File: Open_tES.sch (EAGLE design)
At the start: 61 parts, among them IC2 MAX232ECWES, IC3 4023D, IC4 LP2950CZ-5.0, IC5 OPA277U, IC6 LF444CM, IC7 PIC16F1937P, U1 MIC2288YD5-TR, U2 ICL7660ACPAZ, X1 22-23-2041, X2 057-016-1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

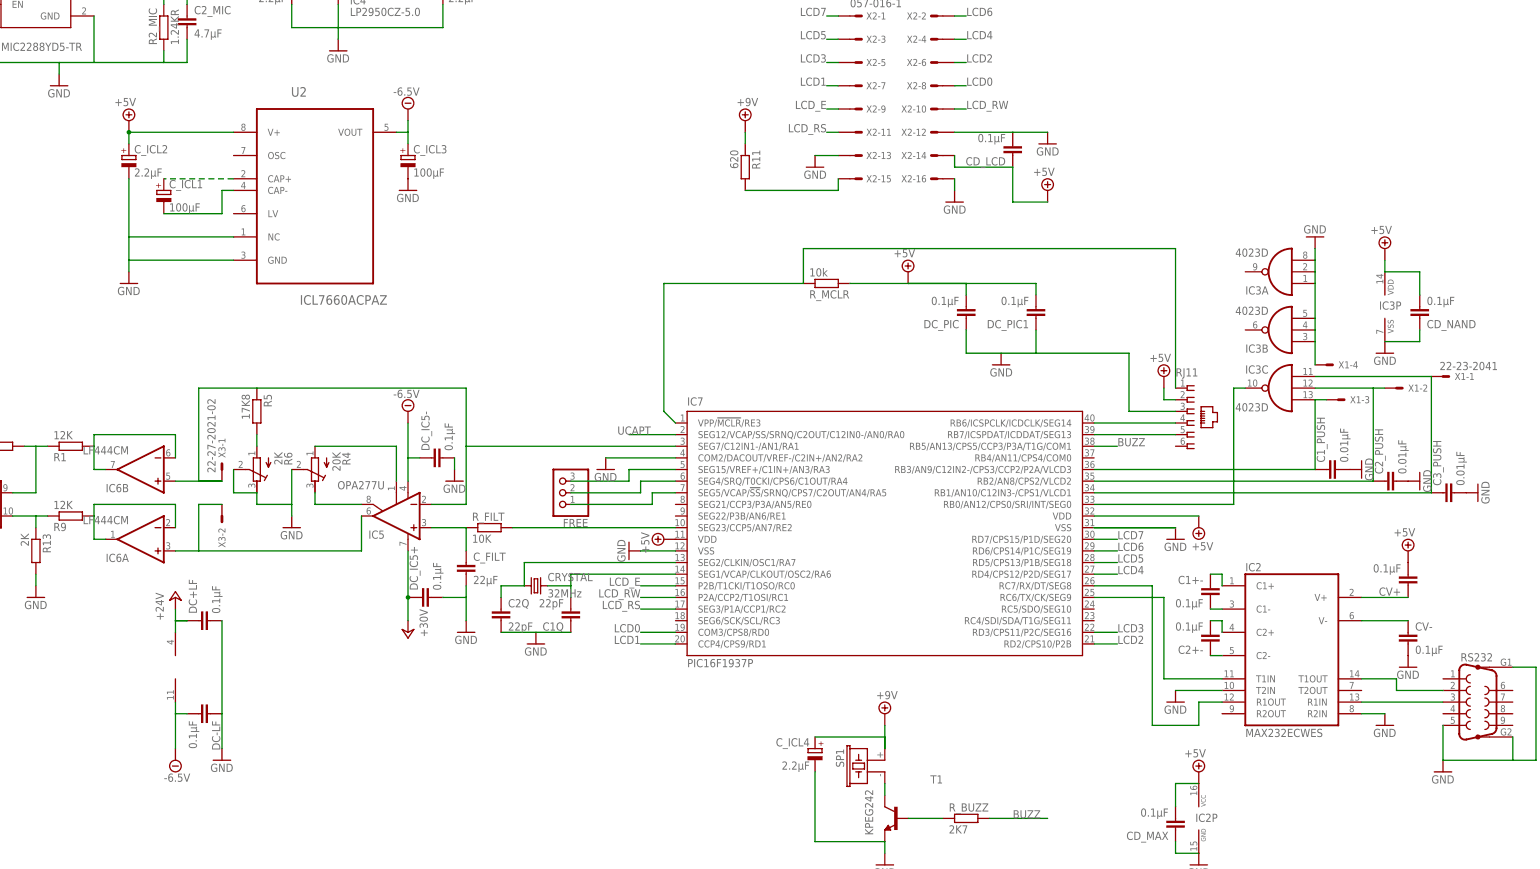
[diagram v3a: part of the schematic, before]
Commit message: use of MAX232 for negative voltage with MIC5270 for regulation (-5V)
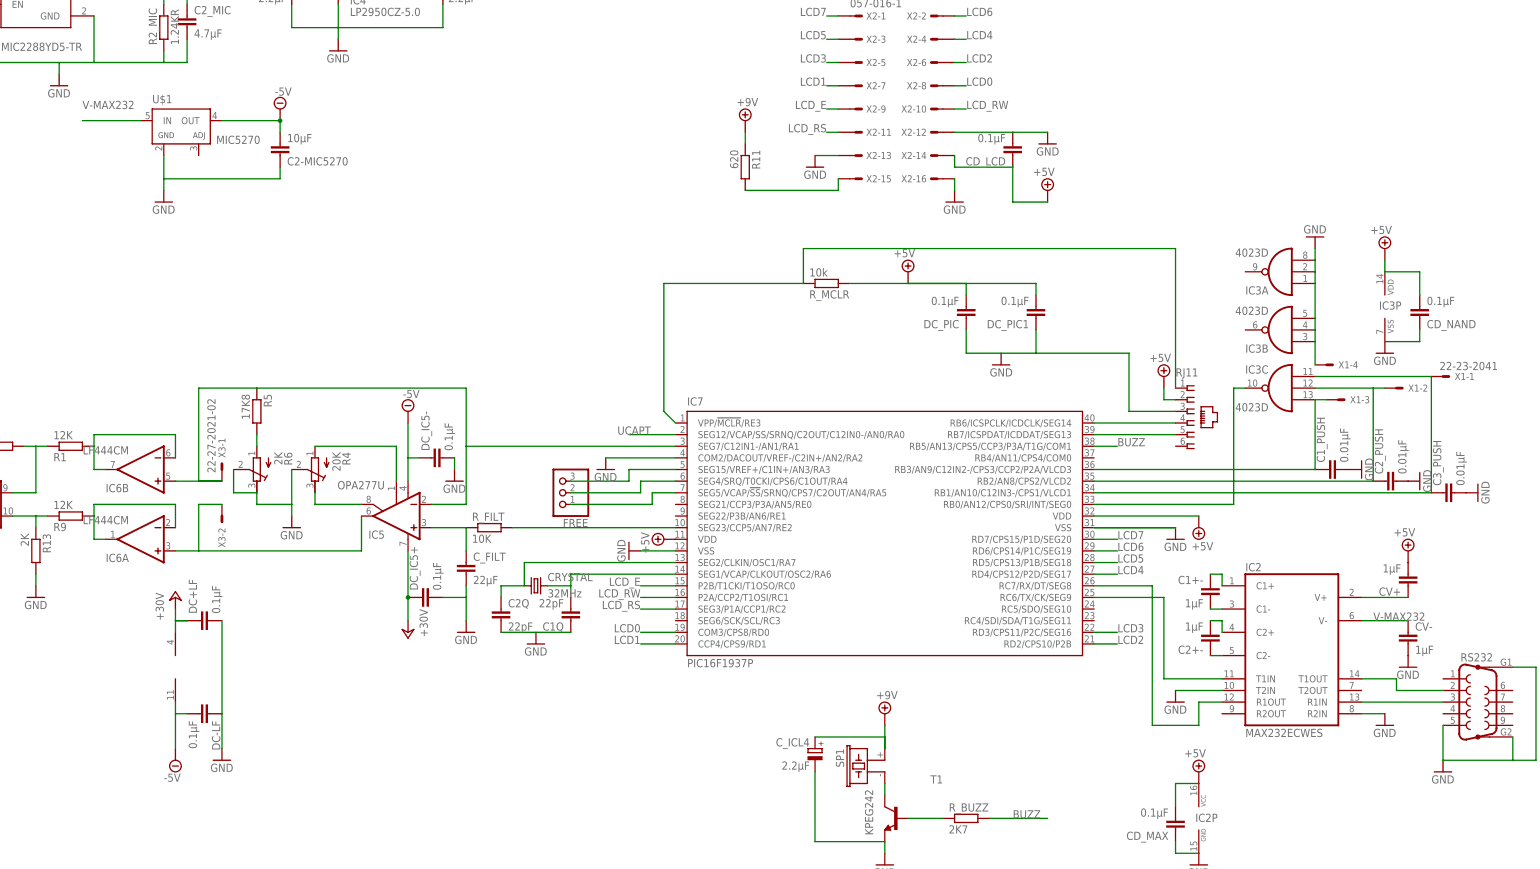
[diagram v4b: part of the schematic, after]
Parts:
- removed C_ICL1, C_ICL3: 100µF, rcl:CPOL-EUE2,5-6E
- removed C_ICL2: 2.2µF, rcl:CPOL-EUE1.8-4
- removed U2: ICL7660ACPAZ, Intersil-ICL7660:ICL7660ACPAZ
- added C2-MIC5270: 10µF, rcl:C-EUC0805
- added U$1: MIC5270, Open_tES:MIC5270
- C1+-, C2+-, CV+, CV-: value 0.1µF -> 1µF; OC_FARNELL 1414664 -> 2496946
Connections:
- removed net N$21: C_ICL1.+, U2.CAP+
- removed net N$27: C_ICL1.-, U2.CAP-
- removed net N$33: CV-.1, IC2G$1.V-
- new net V-MAX232: CV-.1, IC2G$1.V-, U$1.IN
- net +5V/1: no longer C_ICL2.+, U2.V+
- net -5V: now also C2-MIC5270.2, U$1.OUT; no longer C_ICL3.+, U2.VOUT
- net GND: now also C2-MIC5270.1, U$1.GND; no longer C_ICL2.-, C_ICL3.-, U2.GND, U2.NC
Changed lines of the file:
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@@
 <part name="GND13" library="supply1" deviceset="GND" device=""/>
 <part name="GND19" library="supply1" deviceset="GND" device=""/>
-<part name="P+11" library="supply1" deviceset="+24V" device=""/>
+<part name="P+11" library="supply1" deviceset="+24V" device="" value="+30V"/>
 <part name="GND22" library="supply1" deviceset="GND" device=""/>
 <part name="GND25" library="supply1" deviceset="GND" device=""/>
@@
 <attribute name="OC_FARNELL" value="9489479"/>
 </part>
-<part name="U2" library="Intersil-ICL7660" deviceset="ICL7660ACPAZ" device=""/>
-<part name="C_ICL2" library="rcl" deviceset="CPOL-EU" device="E1.8-4" value="2.2µF">
-<attribute name="OC_FARNELL" value="8766983"/>
-</part>
-<part name="GND32" library="supply1" deviceset="GND" device=""/>
-<part name="C_ICL1" library="rcl" deviceset="CPOL-EU" device="E2,5-6E" value="100µF">
-<attribute name="OC_FARNELL" value="9452648"/>
-</part>
-<part name="C_ICL3" library="rcl" deviceset="CPOL-EU" device="E2,5-6E" value="100µF">
-<attribute name="OC_FARNELL" value="9452648"/>
-</part>
-<part name="GND33" library="supply1" deviceset="GND" device=""/>
-<part name="SUPPLY8" library="supply2" deviceset="-5V" device="" value="-6.5V"/>
 <part name="C1_MIC" library="rcl" deviceset="C-EU" device="C0805" value="4.7µF">
 <attribute name="OC_FARNELL" value="2458302"/>
@@
 <attribute name="OC_FARNELL" value="8766983"/>
 </part>
-<part name="SUPPLY3" library="supply2" deviceset="-5V" device="" value="-6.5V"/>
-<part name="SUPPLY9" library="supply2" deviceset="-5V" device="" value="-6.5V"/>
+<part name="SUPPLY3" library="supply2" deviceset="-5V" device="" value="-5V"/>
+<part name="SUPPLY9" library="supply2" deviceset="-5V" device="" value="-5V"/>
 <part name="IC2" library="maxim-6b" deviceset="MAX232ECWE" device="S">
 <attribute name="OC_FARNELL" value="2511968"/>
 </part>
-<part name="CV+" library="rcl" deviceset="C-EU" device="C0805" value="0.1µF">
-<attribute name="OC_FARNELL" value="1414664"/>
-</part>
-<part name="CV-" library="rcl" deviceset="C-EU" device="C0805" value="0.1µF">
-<attribute name="OC_FARNELL" value="1414664"/>
-</part>
-<part name="C2+-" library="rcl" deviceset="C-EU" device="C0805" value="0.1µF">
-<attribute name="OC_FARNELL" value="1414664"/>
-</part>
-<part name="C1+-" library="rcl" deviceset="C-EU" device="C0805" value="0.1µF">
-<attribute name="OC_FARNELL" value="1414664"/>
+<part name="CV+" library="rcl" deviceset="C-EU" device="C0805" value="1µF">
+<attribute name="OC_FARNELL" value="2496946"/>
+</part>
+<part name="CV-" library="rcl" deviceset="C-EU" device="C0805" value="1µF">
+<attribute name="OC_FARNELL" value="2496946"/>
+</part>
+<part name="C2+-" library="rcl" deviceset="C-EU" device="C0805" value="1µF">
+<attribute name="OC_FARNELL" value="2496946"/>
+</part>
+<part name="C1+-" library="rcl" deviceset="C-EU" device="C0805" value="1µF">
+<attribute name="OC_FARNELL" value="2496946"/>
 </part>
 <part name="GND27" library="supply1" deviceset="GND" device=""/>
@@
 <attribute name="OC_FARNELL" value="1469389"/>
 </part>
-<part name="SUPPLY16" library="supply2" deviceset="+5V/1" device="" value="+5V"/>
+<part name="U$1" library="Open_tES" deviceset="MIC5270" device=""/>
+<part name="C2-MIC5270" library="rcl" deviceset="C-EU" device="C0805" value="10µF">
+<attribute name="OC_FARNELL" value="2346934"/>
+</part>
+<part name="GND8" library="supply1" deviceset="GND" device=""/>
+<part name="SUPPLY17" library="supply2" deviceset="-5V" device="" value="-5V"/>
 </parts>
 <sheets>
@@
 <attribute name="OC_FARNELL" x="111.76" y="233.68" size="1.778" layer="96" display="off"/>
 </instance>
-<instance part="U2" gate="A" x="106.68" y="187.96"/>
-<instance part="C_ICL2" gate="G$1" x="66.04" y="193.04">
-<attribute name="OC_FARNELL" x="66.04" y="193.04" size="1.778" layer="96" display="off"/>
-</instance>
-<instance part="GND32" gate="1" x="66.04" y="165.1"/>
-<instance part="C_ICL1" gate="G$1" x="73.66" y="185.42">
-<attribute name="OC_FARNELL" x="73.66" y="185.42" size="1.778" layer="96" display="off"/>
-</instance>
-<instance part="C_ICL3" gate="G$1" x="127" y="193.04">
-<attribute name="OC_FARNELL" x="127" y="193.04" size="1.778" layer="96" display="off"/>
-</instance>
-<instance part="GND33" gate="1" x="127" y="185.42"/>
-<instance part="SUPPLY8" gate="-5V" x="127" y="203.2" rot="R180"/>
 <instance part="C1_MIC" gate="G$1" x="25.4" y="226.06" rot="MR0">
 <attribute name="OC_FARNELL" x="25.4" y="226.06" size="1.778" layer="96" rot="MR0" display="off"/>
@@
 <attribute name="OC_FARNELL" x="66.04" y="243.84" size="1.778" layer="96" display="off"/>
 </instance>
-<instance part="SUPPLY16" gate="G$1" x="66.04" y="200.66"/>
+<instance part="U$1" gate="G1" x="76.2" y="198.12"/>
+<instance part="C2-MIC5270" gate="G$1" x="99.06" y="193.04" rot="MR180">
+<attribute name="OC_FARNELL" x="99.06" y="193.04" size="1.778" layer="96" rot="MR180" display="off"/>
+</instance>
+<instance part="GND8" gate="1" x="73.66" y="182.88"/>
+<instance part="SUPPLY17" gate="-5V" x="99.06" y="203.2" rot="R180"/>
 </instances>
 <busses>
@@
 </segment>
 <segment>
-<pinref part="C_ICL3" gate="G$1" pin="-"/>
-<pinref part="GND33" gate="1" pin="GND"/>
-</segment>
-<segment>
 <pinref part="CV-" gate="G$1" pin="2"/>
 <pinref part="GND27" gate="1" pin="GND"/>
@@
 </segment>
 <segment>
-<pinref part="U2" gate="A" pin="NC"/>
-<pinref part="U2" gate="A" pin="GND"/>
-<pinref part="C_ICL2" gate="G$1" pin="-"/>
-<pinref part="GND32" gate="1" pin="GND"/>
-<wire x1="66.04" y1="167.64" x2="66.04" y2="170.18" width="0.1524" layer="91"/>
-<wire x1="66.04" y1="170.18" x2="66.04" y2="175.26" width="0.1524" layer="91"/>
-<wire x1="66.04" y1="175.26" x2="66.04" y2="187.96" width="0.1524" layer="91"/>
-<wire x1="88.9" y1="170.18" x2="66.04" y2="170.18" width="0.1524" layer="91"/>
-<wire x1="88.9" y1="175.26" x2="66.04" y2="175.26" width="0.1524" layer="91"/>
-</segment>
-<segment>
 <pinref part="GND15" gate="1" pin="GND"/>
 <wire x1="170.18" y1="127" x2="185.42" y2="127" width="0.1524" layer="91"/>
@@
 <pinref part="IC7" gate="G$1" pin="VSS"/>
 <wire x1="177.8" y1="106.68" x2="185.42" y2="106.68" width="0.1524" layer="91"/>
+</segment>
+<segment>
+<pinref part="U$1" gate="G1" pin="GND"/>
+<pinref part="GND8" gate="1" pin="GND"/>
+<wire x1="73.66" y1="185.42" x2="73.66" y2="187.96" width="0.1524" layer="91"/>
+<pinref part="C2-MIC5270" gate="G$1" pin="1"/>
+<wire x1="73.66" y1="187.96" x2="73.66" y2="193.04" width="0.1524" layer="91"/>
+<wire x1="99.06" y1="190.5" x2="99.06" y2="187.96" width="0.1524" layer="91"/>
+<wire x1="99.06" y1="187.96" x2="73.66" y2="187.96" width="0.1524" layer="91"/>
 </segment>
 </net>
@@
 <net name="-5V" class="0">
 <segment>
-<pinref part="U2" gate="A" pin="VOUT"/>
-<pinref part="C_ICL3" gate="G$1" pin="+"/>
-<wire x1="127" y1="195.58" x2="127" y2="198.12" width="0.1524" layer="91"/>
-<wire x1="127" y1="198.12" x2="124.46" y2="198.12" width="0.1524" layer="91"/>
-<pinref part="SUPPLY8" gate="-5V" pin="-5V"/>
-<wire x1="127" y1="198.12" x2="127" y2="200.66" width="0.1524" layer="91"/>
-</segment>
-<segment>
 <pinref part="IC6" gate="P" pin="V-"/>
 <wire x1="76.2" y1="63.5" x2="76.2" y2="71.12" width="0.1524" layer="91"/>
@@
 <wire x1="127" y1="134.62" x2="127" y2="127" width="0.1524" layer="91"/>
 <wire x1="127" y1="127" x2="127" y2="121.92" width="0.1524" layer="91"/>
+</segment>
+<segment>
+<pinref part="U$1" gate="G1" pin="OUT"/>
+<pinref part="C2-MIC5270" gate="G$1" pin="2"/>
+<wire x1="86.36" y1="200.66" x2="99.06" y2="200.66" width="0.1524" layer="91"/>
+<wire x1="99.06" y1="200.66" x2="99.06" y2="198.12" width="0.1524" layer="91"/>
+<pinref part="SUPPLY17" gate="-5V" pin="-5V"/>
+<junction x="99.06" y="200.66"/>
 </segment>
 </net>
@@
 <pinref part="IC7" gate="G$1" pin="VDD"/>
 <pinref part="SUPPLY7" gate="G$1" pin="+5V/1"/>
-</segment>
-<segment>
-<pinref part="U2" gate="A" pin="V+"/>
-<wire x1="66.04" y1="198.12" x2="88.9" y2="198.12" width="0.1524" layer="91"/>
-<pinref part="C_ICL2" gate="G$1" pin="+"/>
-<wire x1="66.04" y1="195.58" x2="66.04" y2="198.12" width="0.1524" layer="91"/>
-<pinref part="SUPPLY16" gate="G$1" pin="+5V/1"/>
-<junction x="66.04" y="198.12"/>
 </segment>
 </net>
@@
 </segment>
 </net>
-<net name="N$21" class="0">
-<segment>
-<pinref part="U2" gate="A" pin="CAP+"/>
-<pinref part="C_ICL1" gate="G$1" pin="+"/>
-<wire x1="88.9" y1="187.96" x2="73.66" y2="187.96" width="0.1524" layer="91" style="longdash"/>
-</segment>
-</net>
-<net name="N$27" class="0">
-<segment>
-<pinref part="U2" gate="A" pin="CAP-"/>
-<wire x1="88.9" y1="185.42" x2="86.36" y2="185.42" width="0.1524" layer="91"/>
-<wire x1="86.36" y1="185.42" x2="86.36" y2="180.34" width="0.1524" layer="91"/>
-<pinref part="C_ICL1" gate="G$1" pin="-"/>
-<wire x1="86.36" y1="180.34" x2="73.66" y2="180.34" width="0.1524" layer="91"/>
-</segment>
-</net>
 <net name="N$20" class="0">
 <segment>
@@
 </segment>
 </net>
-<net name="N$33" class="0">
+<net name="V-MAX232" class="0">
 <segment>
 <pinref part="IC2" gate="G$1" pin="V-"/>
 <pinref part="CV-" gate="G$1" pin="1"/>
 <wire x1="345.44" y1="91.44" x2="335.28" y2="91.44" width="0.1524" layer="91"/>
-</segment>
-</net>
+<label x="337.82" y="91.44" size="1.778" layer="95"/>
+</segment>
+<segment>
+<pinref part="U$1" gate="G1" pin="IN"/>
+<wire x1="68.58" y1="200.66" x2="55.88" y2="200.66" width="0.1524" layer="91"/>
+<label x="55.88" y="203.2" size="1.778" layer="95"/>
+</segment>
+</net>

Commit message: Changing of RJ connector with 90deg connector to ease PIC programming. Need a new hole in back end plate
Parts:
- RJ11: value (none) -> RJ11-2L-B; device con-amp:520425-3 -> con-tycoelectronics:RJ11-2L-B; OC_FARNELL 3938414 -> 3938359
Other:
- moved on the sheet: RJ11
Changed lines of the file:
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@@
 </part>
 <part name="GND1" library="supply1" deviceset="GND" device=""/>
-<part name="RJ11" library="con-amp" deviceset="520425-3" device="">
-<attribute name="OC_FARNELL" value="3938414"/>
+<part name="RJ11" library="con-tycoelectronics" deviceset="RJ11" device="" technology="-2L-B" value="RJ11-2L-B">
+<attribute name="OC_FARNELL" value="3938359"/>
 </part>
 <part name="R_MCLR" library="rcl" deviceset="R-EU_" device="0204/7" value="10k">

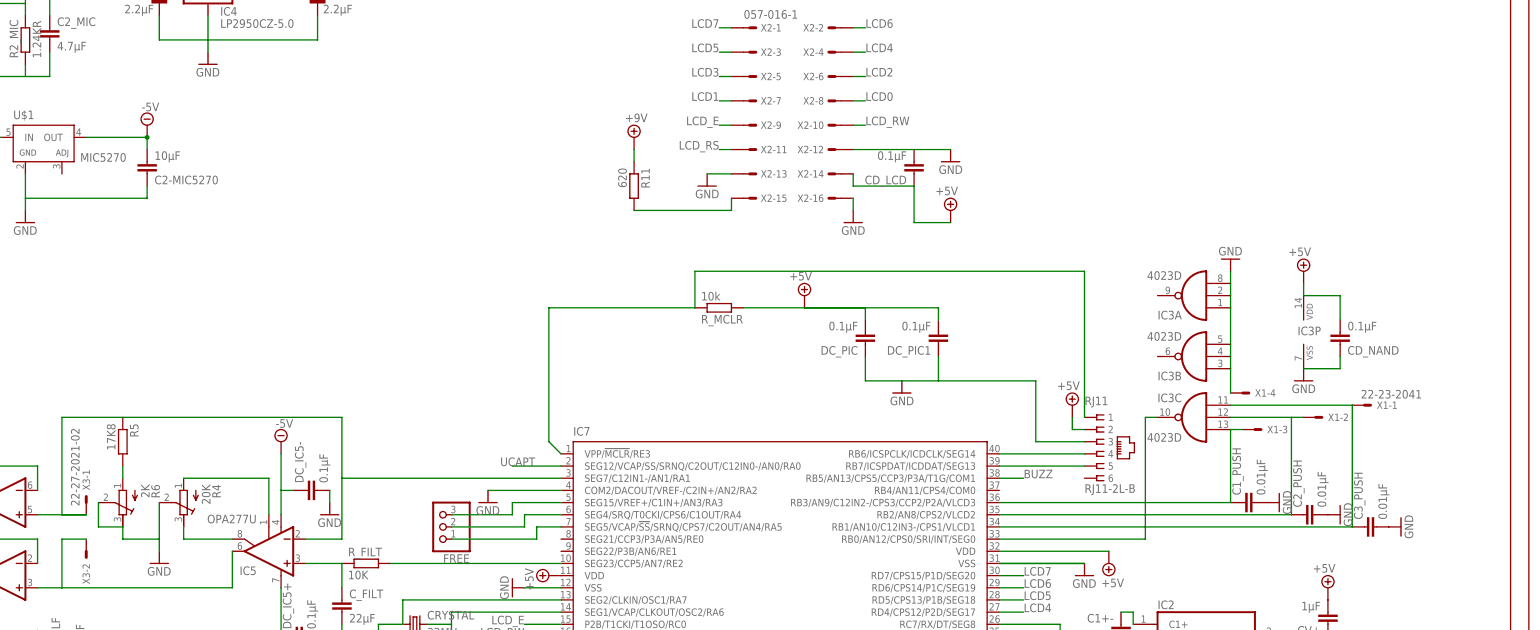
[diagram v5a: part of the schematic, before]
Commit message: 1)replace 4023 triple 3-input NAND with 74LVC1G10W6-7 simple 3-input NAND 2) solve consistent problem between sch and brd
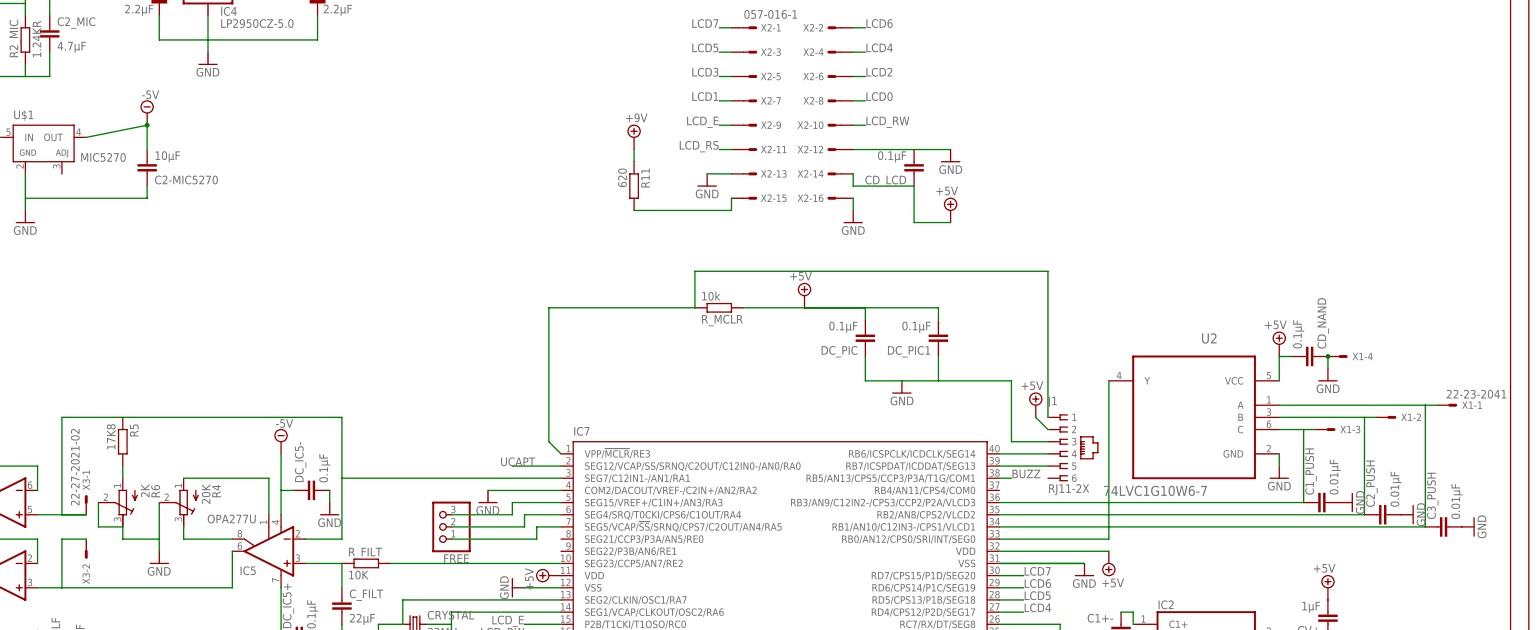
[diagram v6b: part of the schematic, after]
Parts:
- removed IC3: 4023D, 40xx:4023D
- removed RJ11: RJ11-2L-B, con-tycoelectronics:RJ11-2L-B
- added J1: RJ11-2X, con-tycoelectronics:RJ11-2X
- added U2: 74LVC1G10W6-7, Open_tES:74LVC1G10W6-7
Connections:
- net +5V/1: now also J1.2, U2.VCC; no longer IC3P.VDD, RJ11.2
- net GND: now also J1.3, U2.GND; no longer IC3A.I0, IC3A.I1, IC3A.I2, IC3B.I0, IC3B.I1, IC3B.I2, IC3P.VSS, RJ11.3
- net MCLR: now also J1.1; no longer RJ11.1
- net N$18: now also U2.C; no longer IC3C.I2
- net N$23: now also U2.B; no longer IC3C.I1
- net N$25: now also U2.Y; no longer IC3C.O
- net N$9: now also U2.A; no longer IC3C.I0
- net PGC: now also J1.5; no longer RJ11.5
- net PGD: now also J1.4; no longer RJ11.4
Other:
- moved on the sheet: C1_PUSH, C2_PUSH, C3_PUSH, CD_NAND, X1-1, X1-2, X1-3, X1-4

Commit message: update version on the schem and board -2.0-
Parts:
- U$4: VERSION 1.0 -> 2.0
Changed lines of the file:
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@@
 <part name="GND7" library="supply1" deviceset="GND" device=""/>
 <part name="U$4" library="Open_tES" deviceset="FRAME" device="">
-<attribute name="VERSION" value="1.0"/>
+<attribute name="VERSION" value="2.0"/>
 </part>
 <part name="U1" library="Open_tES" deviceset="MIC2288YD5-TR" device="">
